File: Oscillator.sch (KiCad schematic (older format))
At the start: 0 parts

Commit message: Version control test
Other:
- note added: "version 2\nasdfasdf"
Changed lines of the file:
@@
 F1 "main.sch" 50
 $EndSheet
+Text Notes 3900 3850 0    50   ~ 0
+version 2\nasdfasdf
 $EndSCHEMATC

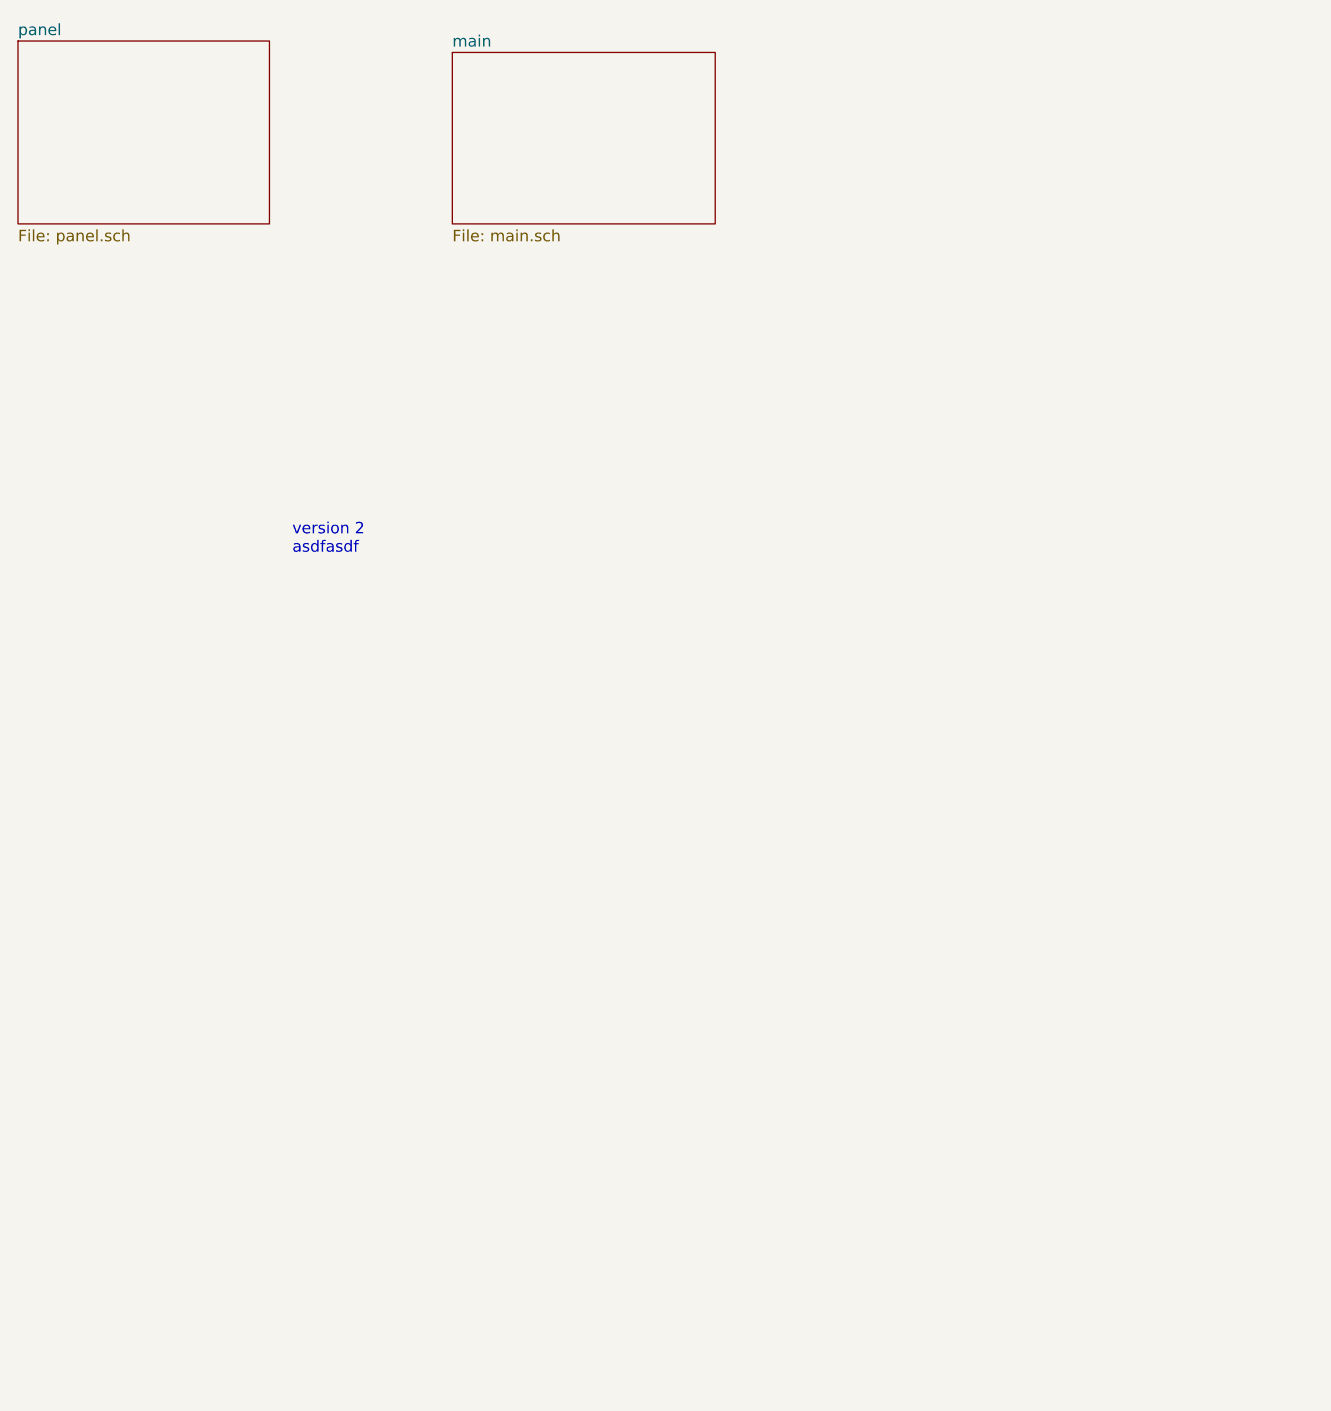
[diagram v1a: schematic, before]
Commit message: Added version markings
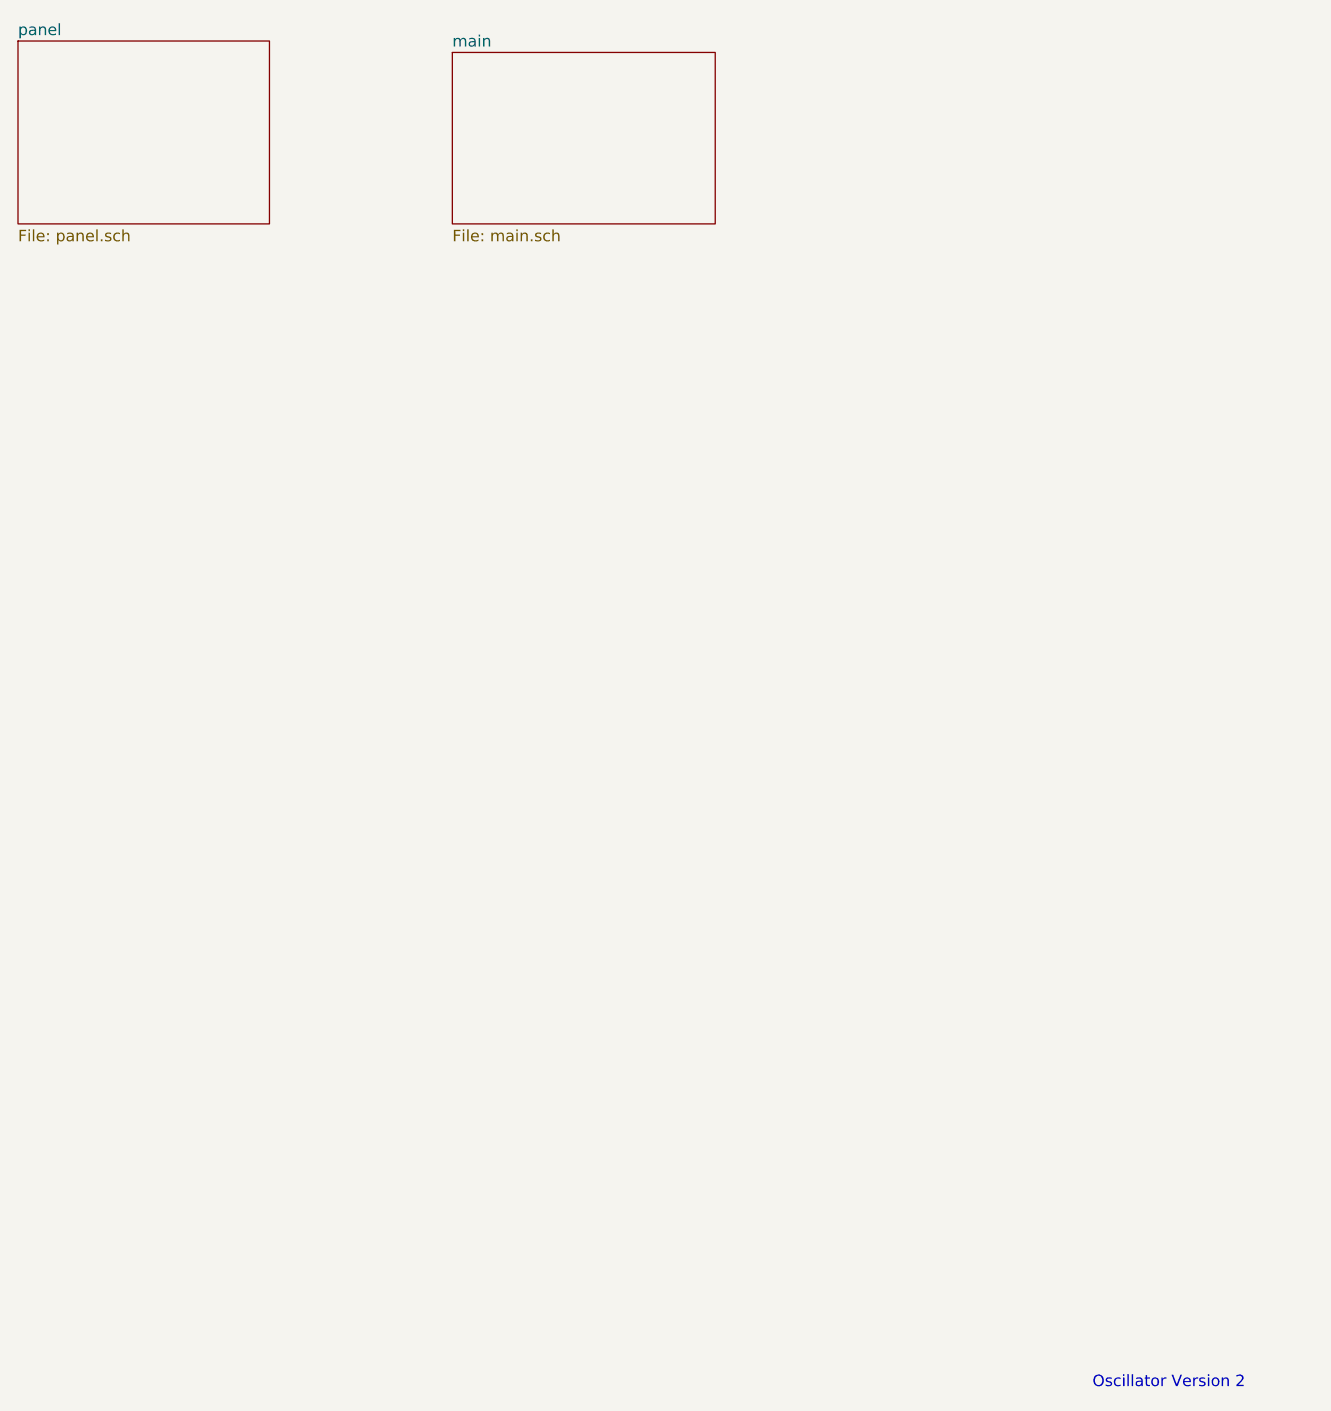
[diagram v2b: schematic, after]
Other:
- note added: "Oscillator Version 2"
- note removed: "version 2\nasdfasdf"
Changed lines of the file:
@@
 F1 "main.sch" 50
 $EndSheet
-Text Notes 3900 3850 0    50   ~ 0
-version 2\nasdfasdf
+Text Notes 7400 7500 0    50   ~ 0
+Oscillator Version 2
 $EndSCHEMATC
